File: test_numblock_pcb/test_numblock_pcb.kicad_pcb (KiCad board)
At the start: 2 copper layers, 55 parts, among them J1 AVR-ISP-6, J2 USB4105GFA120, SW1 SW_Push, SW10 SW_Push, SW11 SW_Push, SW12 SW_Push, SW13 SW_Push, SW14 SW_Push, SW15 SW_Push, SW16 SW_Push, SW17 SW_Push, SW18 SW_Push, SW2 SW_Push, SW3 SW_Push, SW4 SW_Push, SW5 SW_Push, SW6 SW_Push, SW7 SW_Push, SW8 SW_Push, SW9 SW_Push, U1 ATmega32U4-A, Y1 16MHz

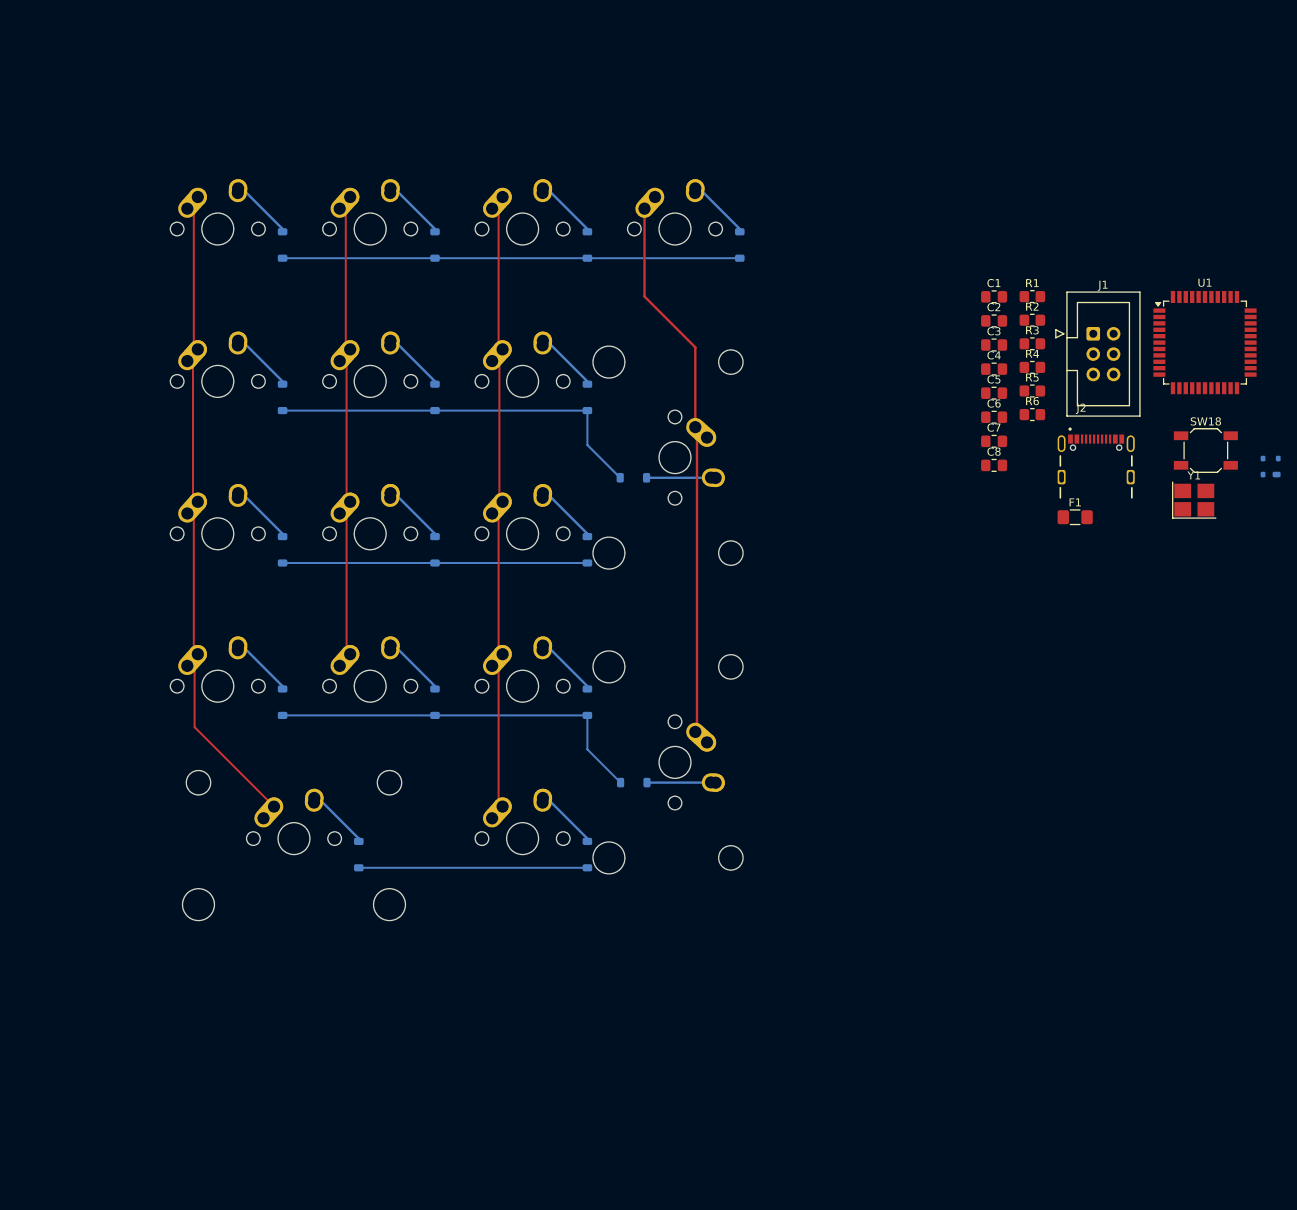
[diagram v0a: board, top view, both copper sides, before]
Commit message: place most components on prototype numblock board
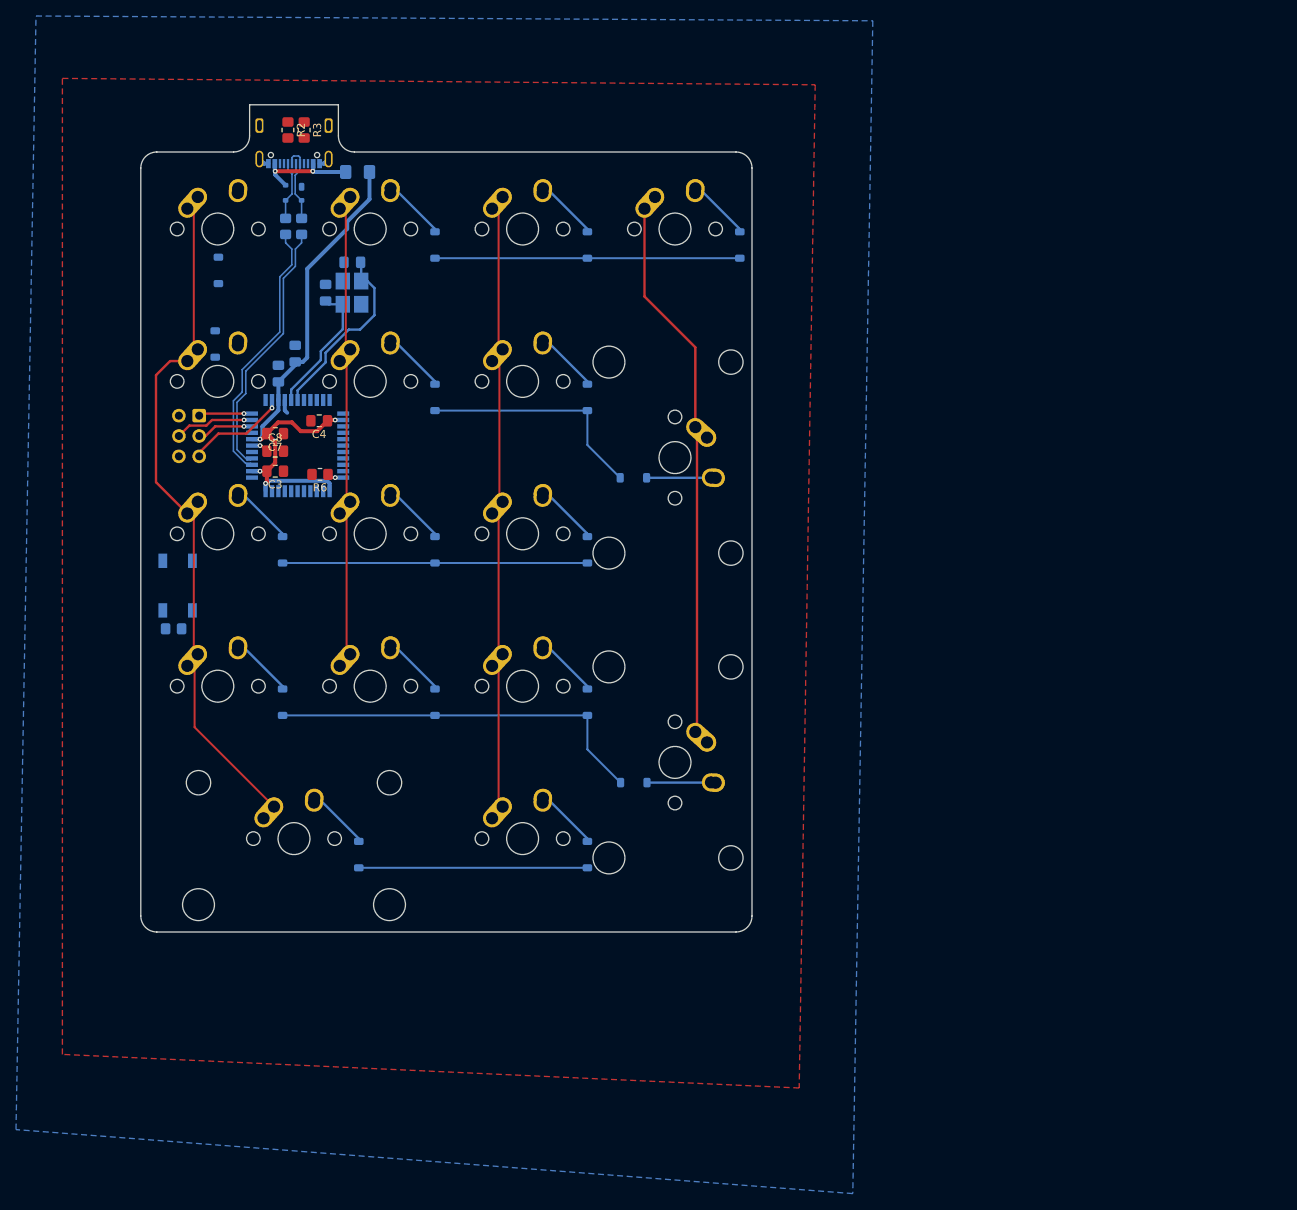
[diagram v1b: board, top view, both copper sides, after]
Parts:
- C1, C2, C5, C6, F1, J1, J2, R1, R4, R5, SW18, U1, Y1: moved to B.Cu
- moved SW18 129.6 mm to (33.1, 82.7), turned to 90 degrees
- moved D18 126.8 mm to (47.6, 33.6), turned to 180 degrees
- moved R1 115.1 mm to (32.6, 88.1), turned to 180 degrees
- moved U1 114.2 mm to (48.1, 65.2)
- moved J1 112.2 mm to (35.8, 61.4), turned to 180 degrees
- moved J2 109.5 mm to (47.6, 25.2)
- moved Y1 108.4 mm to (54.9, 46.1), turned to -90 degrees
- moved F1 99.5 mm to (55.6, 31.0)
- moved R2 96.0 mm to (46.9, 25.7), turned to -90 degrees
- moved R4 95.0 mm to (46.6, 37.8), turned to 90 degrees
- moved R3 94.9 mm to (48.9, 25.7), turned to -90 degrees
- moved R5 93.6 mm to (48.6, 37.8), turned to 90 degrees
- moved C3 91.2 mm to (45.3, 68.4), turned to 180 degrees
- moved C8 89.9 mm to (45.3, 65.9)
- moved C7 89.9 mm to (45.3, 63.7), turned to 180 degrees
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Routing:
- net +5V: track 0.00 -> 72.2 mm, vias 0 -> 4
- net /D-: track 0.00 -> 33.5 mm
- net /D+: track 0.00 -> 32.7 mm
- net Net-(U1-XTAL1): track 0.00 -> 23.2 mm
- net ROW1: track 57.1 -> 38.1 mm
- net ROW2: track 48.2 -> 29.1 mm
- net Net-(U1-XTAL2): track 0.00 -> 17.0 mm
- net Net-(D18-VCC): track 0.00 -> 13.1 mm, vias 0 -> 2
- net Net-(J1-~{RST}): track 0.00 -> 12.9 mm, vias 0 -> 1
- net /DR+: track 0.00 -> 10.1 mm
- net /MOSI: track 0.00 -> 9.97 mm, vias 0 -> 1
- net /DR-: track 0.00 -> 8.85 mm
- net Net-(D5-A): track 8.01 -> 0.48 mm
- net Net-(D1-A): track 8.01 -> 0.48 mm
- net /SCK: track 0.00 -> 7.10 mm, vias 0 -> 1
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- added copper zone on B.Cu, net GND
- added copper zone on F.Cu, net GND
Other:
- board outline added: 76.4 x 103.4 mm

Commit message: complete the prototype numpad pcb
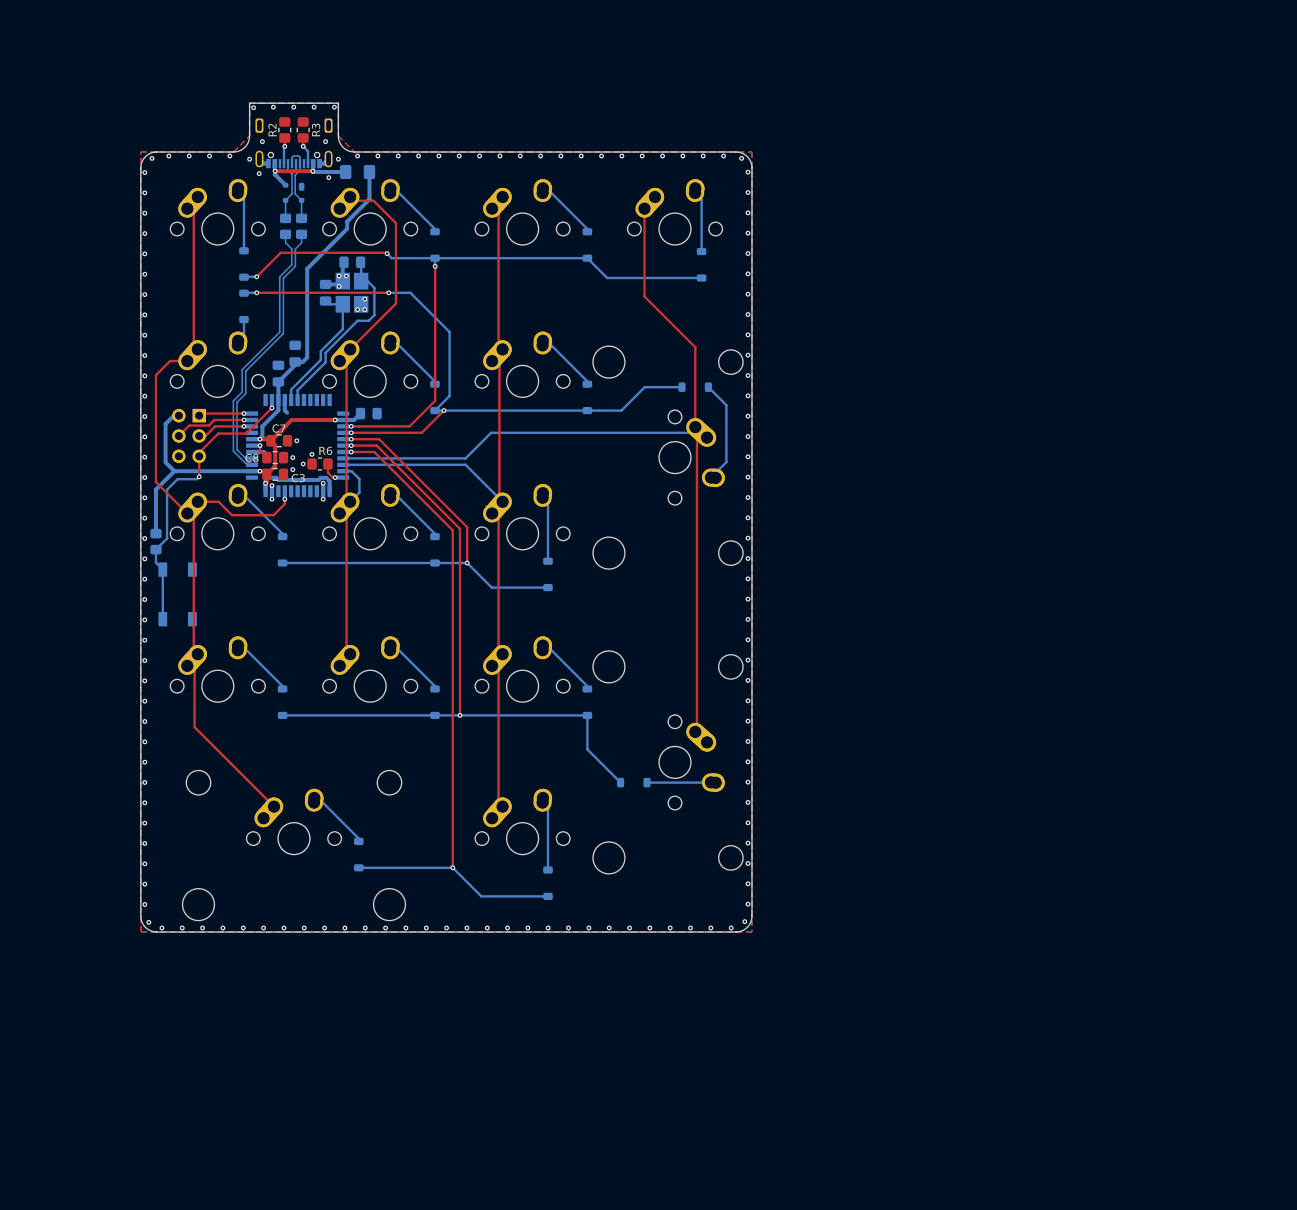
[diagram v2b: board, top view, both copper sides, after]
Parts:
- C4: moved to B.Cu
- J1: footprint Connector_IDC:IDC-Header_2x03_P2.54mm_Vertical -> Connector_PinHeader_2.54mm:PinHeader_2x03_P2.54mm_Vertical
- moved D8 13.7 mm to (97.8, 57.9)
- moved R1 11.1 mm to (30.4, 77.2), turned to -90 degrees
- moved C4 6.26 mm to (57.0, 61.2), turned to 0 degrees
- moved D17 6.09 mm to (79.4, 119.9)
- moved D5 5.92 mm to (41.4, 47.8), turned to -90 degrees
- moved D11 5.81 mm to (79.4, 81.3)
- moved D4 5.38 mm to (98.6, 42.6)
- moved D1 3.30 mm to (41.4, 42.5)
- moved R6 1.30 mm to (50.9, 67.5)
- moved SW18 1.10 mm to (33.1, 83.8)
- moved C7 1.03 mm to (45.8, 64.6)
- moved C8 0.80 mm to (45.3, 66.7)
- moved C3 0.40 mm to (45.3, 68.8)
- moved R2 0.39 mm to (46.5, 25.7)
- moved R3 0.12 mm to (48.8, 25.7)
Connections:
- U1 pad 25: unconnected-(U1-PD4-Pad25) -> ROW1
- U1 pad 26: unconnected-(U1-PD6-Pad26) -> ROW2
- U1 pad 27: unconnected-(U1-PD7-Pad27) -> ROW3
- U1 pad 28: unconnected-(U1-PB4-Pad28) -> ROW4
- U1 pad 29: unconnected-(U1-PB5-Pad29) -> ROW5
- U1 pad 30: unconnected-(U1-PB6-Pad30) -> COL4
- U1 pad 31: unconnected-(U1-PC6-Pad31) -> COL3
- U1 pad 32: unconnected-(U1-PC7-Pad32) -> COL2
- U1 pad 41: unconnected-(U1-PF0-Pad41) -> COL1
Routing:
- net ROW5: track 28.6 -> 85.1 mm, vias 0 -> 2
- net ROW2: track 29.1 -> 84.2 mm, vias 0 -> 4
- net ROW1: track 38.1 -> 90.4 mm, vias 0 -> 4
- net COL4: track 69.0 -> 114.6 mm
- net ROW4: track 48.2 -> 90.5 mm, vias 0 -> 2
- net +5V: track 72.2 -> 101.1 mm
- net Net-(J1-~{RST}): track 12.9 -> 37.2 mm, vias 1 -> 2
- net COL3: track 77.8 -> 99.6 mm
- net ROW3: track 38.1 -> 59.0 mm, vias 0 -> 2
- net COL1: track 87.5 -> 101.3 mm, vias 0 -> 1
- net COL2: track 58.4 -> 69.8 mm
- net GND: track 4.44 -> 13.7 mm, vias 0 -> 156
- net Net-(D1-A): track 0.48 -> 8.03 mm
- net Net-(D8-A): track 8.06 -> 13.0 mm
- net Net-(J2-CC2): track 0.00 -> 3.45 mm, vias 0 -> 1
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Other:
- board size 76.4 x 103.4 mm -> 76.4 x 103.6 mm
